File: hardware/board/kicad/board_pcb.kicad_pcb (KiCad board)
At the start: 2 copper layers, 123 x 66.6 mm, 15 parts, among them J1 MEGA BOTTOM, J1 N64_Slot, J2 MEGA TOP, J5 MEGA SIDE

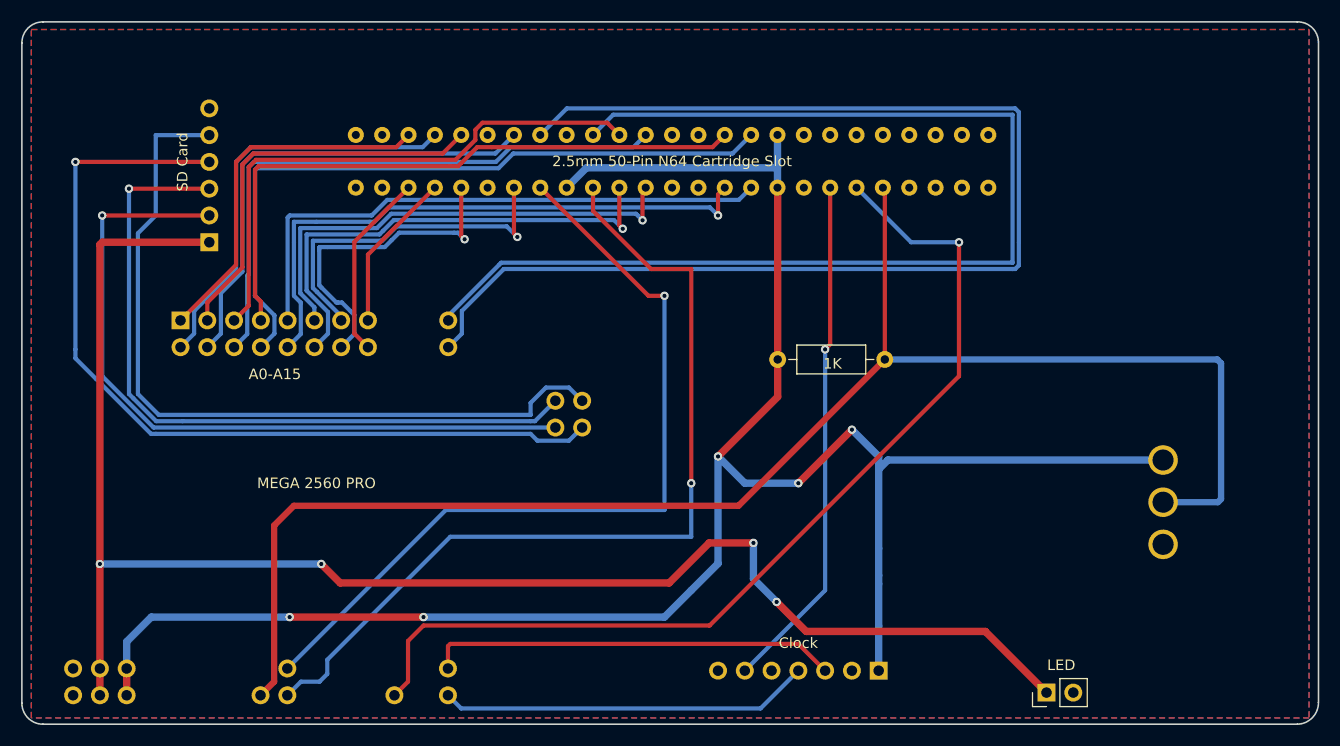
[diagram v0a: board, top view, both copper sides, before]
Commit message: V2 launch: integrated repo with docs, cleanup, and validation
- Firmware: RP2040 headless firmware with GameShark and utils support
- Host tools: Python CLI, validation matrix, Web Serial UI
- Hardware: V2 KiCad project with gerbers, fabrication outputs, custom footprint library
- Enclosure: FreeCAD source and STL for V2 board case
- Docs: README, GETTING_STARTED, HARDWARE, WEB_SERIAL_UI, V1_LEGACY,
  CREDITS_AND_PRIOR_ART, KNOWN_LIMITATIONS, LICENSING, VALIDATION,
  MANUFACTURING_TEST
- Licensing: GPL-3.0 and BSD-2-Clause texts, root LICENSE pointer
- Removed legacy: ATmega2560 firmware, pico-cli skeleton, shield/adapter
  KiCad projects, shield enclosure, bench-only scripts
- Consolidated n64.txt cart catalog to host-tools/ (shared by Python and Web UI)
- Fixed Python imports for integrated repo layout

Validated on two units: SRAM round-trip (1080 Snowboarding) and
EEPROM round-trip (GoldenEye) both PASS.
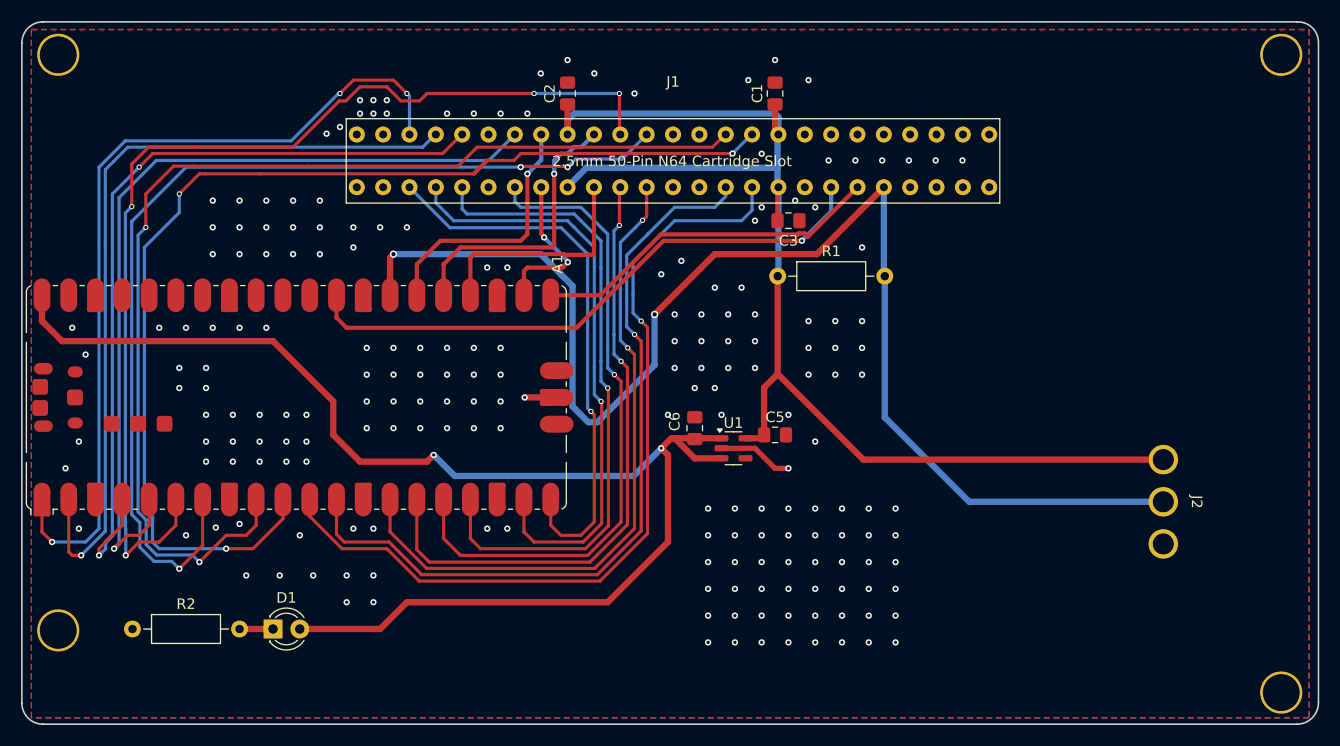
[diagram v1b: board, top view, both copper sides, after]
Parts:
- removed the ? at (208.5, 126.5)
- removed the ? at (208.5, 130.5)
- removed the ? at (208.5, 122.5)
- removed Clock: 01x07, Connector_PinHeader_2.54mm:PinHeader_1x07_P2.54mm_Vertical
- removed the J1 at (131.7, 99.1)
- removed the J1 at (153.1, 144.7)
- removed J5: MEGA SIDE, Connector_PinSocket_2.54mm:PinSocket_2x03_P2.54mm_Vertical
- removed LED: 1x02, Connector_PinHeader_2.54mm:PinHeader_1x02_P2.54mm_Vertical
- removed SD Card: 01x06, Connector_PinHeader_2.54mm:PinHeader_1x06_P2.54mm_Vertical
- added A1: RaspberryPi_Pico, Module:RaspberryPi_Pico_SMD, F.Cu at (126.0, 119.0)
- added C1: 0.1uF, Capacitor_SMD:C_0805_2012Metric_Pad1.18x1.45mm_HandSolder, F.Cu at (171.4, 90.2)
- added C2: 0.1uF, Capacitor_SMD:C_0805_2012Metric_Pad1.18x1.45mm_HandSolder, F.Cu at (151.8, 90.2)
- added C3: 0.1uF, Capacitor_SMD:C_0805_2012Metric_Pad1.18x1.45mm_HandSolder, F.Cu at (172.7, 102.2)
- added C5: 10uF, Capacitor_SMD:C_0805_2012Metric_Pad1.18x1.45mm_HandSolder, F.Cu at (171.4, 122.6)
- added C6: 4.7uF, Capacitor_SMD:C_0805_2012Metric_Pad1.18x1.45mm_HandSolder, F.Cu at (163.8, 121.9)
- added D1: LED, LED_THT:LED_D3.0mm, F.Cu at (123.8, 141.0)
- added J1: N64_Slot, project_footprints:N64_Slot, F.Cu at (131.8, 99.1)
- added R2: 1k, Resistor_THT:R_Axial_DIN0207_L6.3mm_D2.5mm_P10.16mm_Horizontal, F.Cu at (110.5, 141.0)
- added U1: AP2112K-3.3, Package_TO_SOT_SMD:SOT-23-5, F.Cu at (167.5, 123.8)
- J2: value MEGA TOP -> N64_Controller; footprint Connector_PinSocket_2.54mm:PinSocket_2x16_P2.54mm_Vertical -> project_footprints:Controller_Port_3Pin; moved to F.Cu
- R1: value 1K -> 1k
- moved J2 57.8 mm to (208.3, 128.9), turned to 0 degrees
- moved R1 7.90 mm to (171.7, 107.5)
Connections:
- R1 pad 1: +3V3 -> +3.3V
- R1 pad 2: D7 -> JOY_EE_DATA
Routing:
- net +3V3: track 195.2 -> 0.00 mm, vias 5 -> 0
- net D7: track 148.3 -> 0.00 mm
- net JOY_EE_DATA: track 0.00 -> 128.6 mm, vias 0 -> 2
- net +3.3V: track 0.00 -> 124.5 mm
- net D37: track 119.7 -> 0.00 mm
- net D36: track 110.7 -> 0.00 mm
- net ADBUS_7: track 0.00 -> 106.9 mm, vias 0 -> 3
- net ADBUS_6: track 0.00 -> 106.1 mm, vias 0 -> 2
- net ADBUS_4: track 0.00 -> 99.8 mm, vias 0 -> 4
- net ADBUS_5: track 0.00 -> 95.6 mm, vias 0 -> 3
- net D17: track 92.9 -> 0.00 mm, vias 1 -> 0
- net D9: track 84.5 -> 0.00 mm, vias 1 -> 0
- net D52: track 83.2 -> 0.00 mm, vias 1 -> 0
- net ADBUS_0: track 0.00 -> 80.8 mm, vias 0 -> 3
- net ADBUS_3: track 0.00 -> 80.2 mm, vias 0 -> 1
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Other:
- board text removed: "1K"
- board text removed: "A0-A15"
- board text removed: "MEGA 2560 PRO"
